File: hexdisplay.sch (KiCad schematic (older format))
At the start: 6 parts

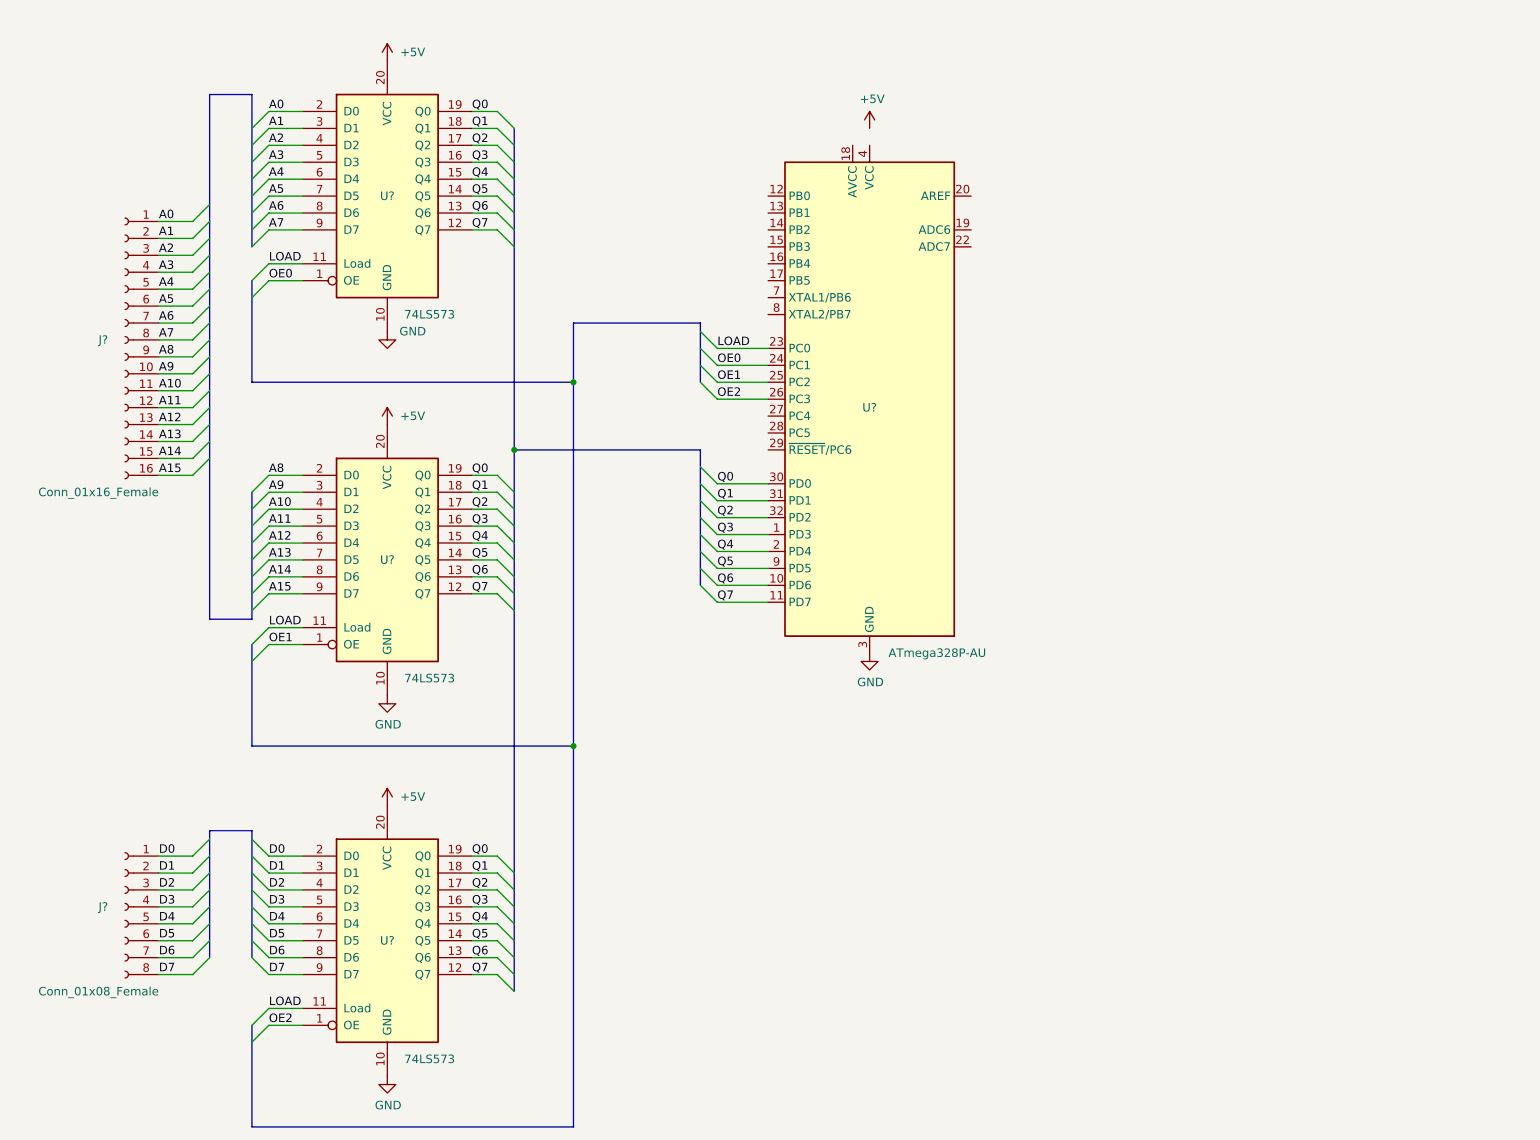
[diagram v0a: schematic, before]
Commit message: Using the Arduino Nano after all; need to finish pinout of pin header connectors
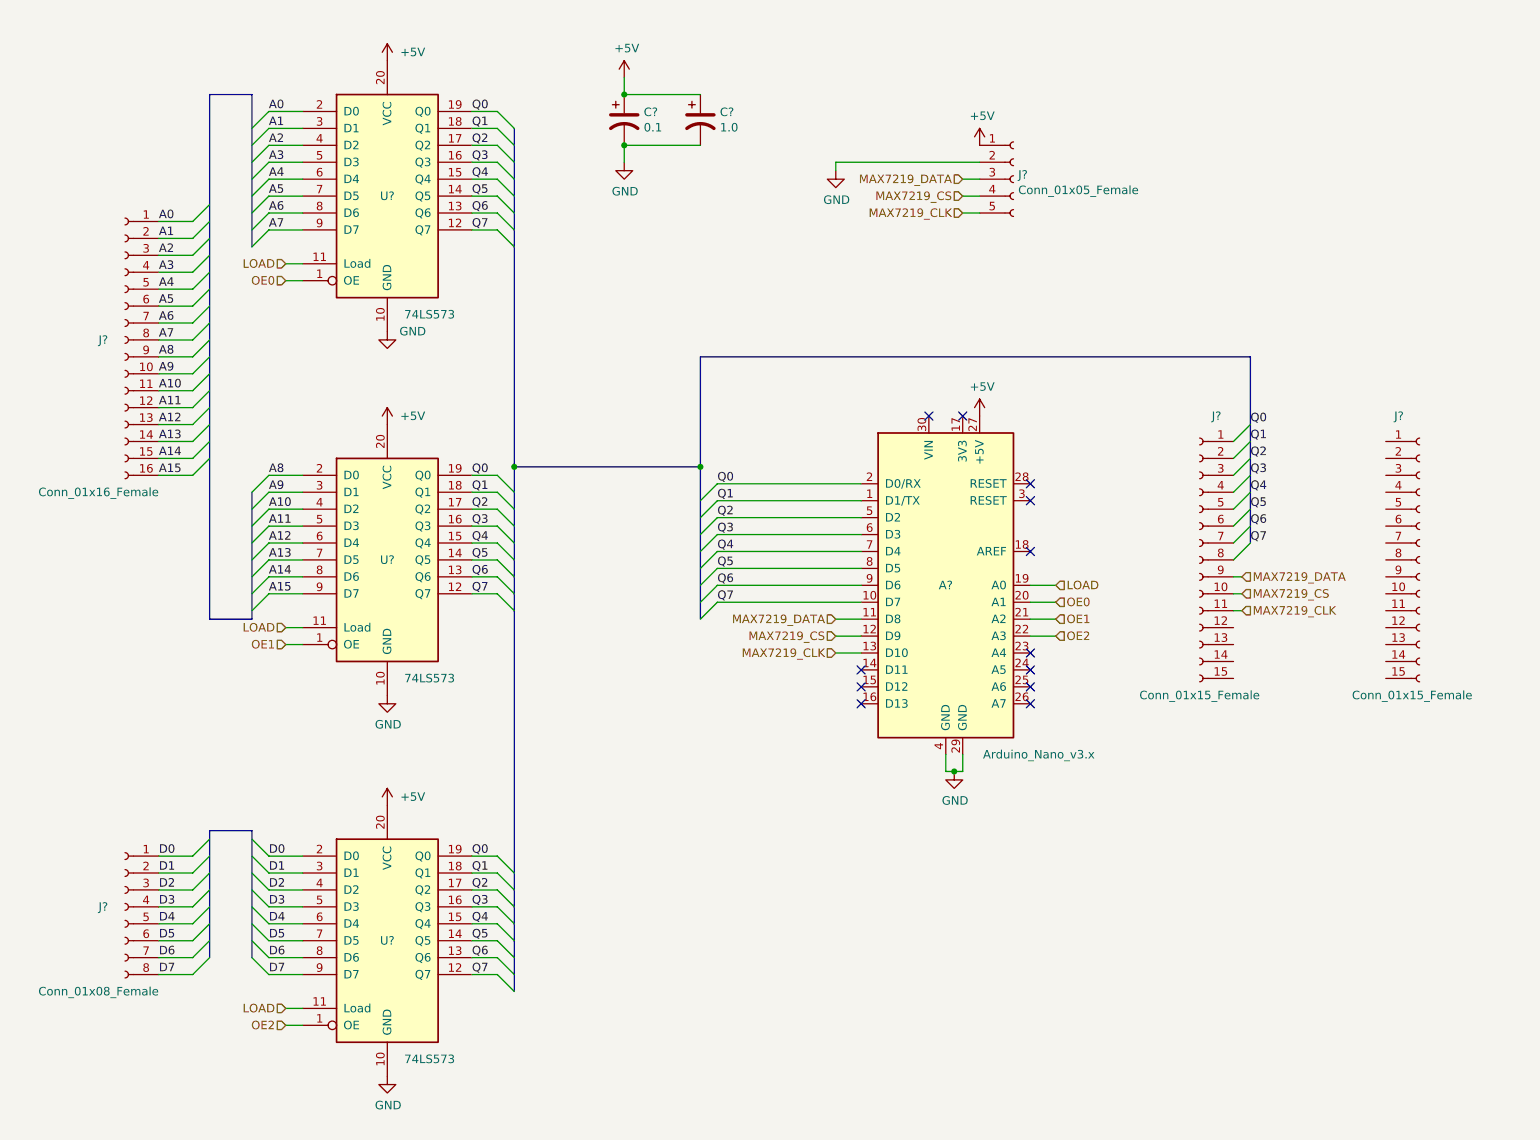
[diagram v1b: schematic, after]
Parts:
- removed U?: ATmega328P-AU, Package_QFP:TQFP-32_7x7mm_P0.8mm, symbol MCU_Microchip_ATmega:ATmega328P-AU
- added A?: Arduino_Nano_v3.x, Module:Arduino_Nano, symbol MCU_Module:Arduino_Nano_v3.x
- added C?: 0.1, symbol Device:CP1
- added C?: 1.0, symbol Device:CP1
- added J?: Conn_01x05_Female, symbol Connector:Conn_01x05_Female
- added J? (x2): Conn_01x15_Female, symbol Connector:Conn_01x15_Female
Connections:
- net +5V: now also A?.27 (+5V), C?.1, C?.1, J?.1 (Pin_1)
- net GND: now also A?.29 (GND), A?.4 (GND), C?.2, C?.2, J?.2 (Pin_2)
- net LOAD: now also A?.19 (A0)
- net OE0: now also A?.20 (A1)
- net OE1: now also A?.21 (A2)
- net OE2: now also A?.22 (A3)
- net Q0: now also A?.2 (D0/RX)
- net Q1: now also A?.1 (D1/TX)
- net Q2: now also A?.5 (D2)
- net Q3: now also A?.6 (D3)
- net Q4: now also A?.7 (D4)
- net Q5: now also A?.8 (D5)
- net Q6: now also A?.9 (D6)
- net Q7: now also A?.10 (D7)
- new net MAX7219_CLK: A?.13 (D10), J?.11 (Pin_11), J?.5 (Pin_5)
- new net MAX7219_CS: A?.12 (D9), J?.10 (Pin_10), J?.4 (Pin_4)
- new net MAX7219_DATA: A?.11 (D8), J?.3 (Pin_3), J?.9 (Pin_9)
- no-connect marks 0 -> 12

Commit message: Everything wired up but ERC fails due to pins not being driven. Have some stuff to learn about hierarchical labels, I think.
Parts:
- removed C?: 0.1, symbol Device:CP1
- added C1, C2, C3: 0.1, symbol Device:CP1
- C4: renamed from C?; value 1.0 -> 10.0
- gave numbers to parts that had none: 9
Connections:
- net +5V: now also J5.4 (Pin_4), C1.1, C2.1, C3.1
- net A4: now also A1.23 (A4), J5.8 (Pin_8)
- net A5: now also A1.24 (A5), J5.7 (Pin_7)
- net A6: now also A1.25 (A6), J5.6 (Pin_6)
- net A7: now also A1.26 (A7), J5.5 (Pin_5)
- net GND: now also J4.3 (Pin_3), J4.4 (Pin_4), J5.2 (Pin_2), C1.2, C2.2, C3.2
- net LOAD: now also J5.12 (Pin_12)
- net MAX7219_CLK: now also J4.13 (Pin_13); no longer J4.11 (Pin_11)
- net MAX7219_CS: now also J4.12 (Pin_12); no longer J4.10 (Pin_10)
- net MAX7219_DATA: now also J4.11 (Pin_11); no longer J4.9 (Pin_9)
- net OE0: now also J5.11 (Pin_11)
- net OE1: now also J5.10 (Pin_10)
- net OE2: now also J5.9 (Pin_9)
- net D11: now reaches A1.14 (D11)
- net D11: now also J4.14 (Pin_14)
- net D12: now reaches A1.15 (D12)
- net D12: now also J4.15 (Pin_15)
- net D13: now reaches A1.16 (D13)
- net D13: now also J5.15 (Pin_15)
- net +3V3: now reaches A1.17 (3V3)
- net +3V3: now also J5.14 (Pin_14)
- net AREF: now reaches A1.18 (AREF)
- net AREF: now also J5.13 (Pin_13)
- net RESET: now reaches A1.28 (RESET)
- net RESET: now also A1.3 (RESET), J5.3 (Pin_3)
- net VIN: now reaches A1.30 (VIN)
- net VIN: now also J5.1 (Pin_1)
- no-connect marks 12 -> 0
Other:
- moved on the sheet: C4, J3, J4, J5
